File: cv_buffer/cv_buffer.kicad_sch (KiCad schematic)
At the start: 8 parts, among them J1 CV connector, J2 Pot connector, U1 HT7550-1, U2 TLV6001UIDBVR

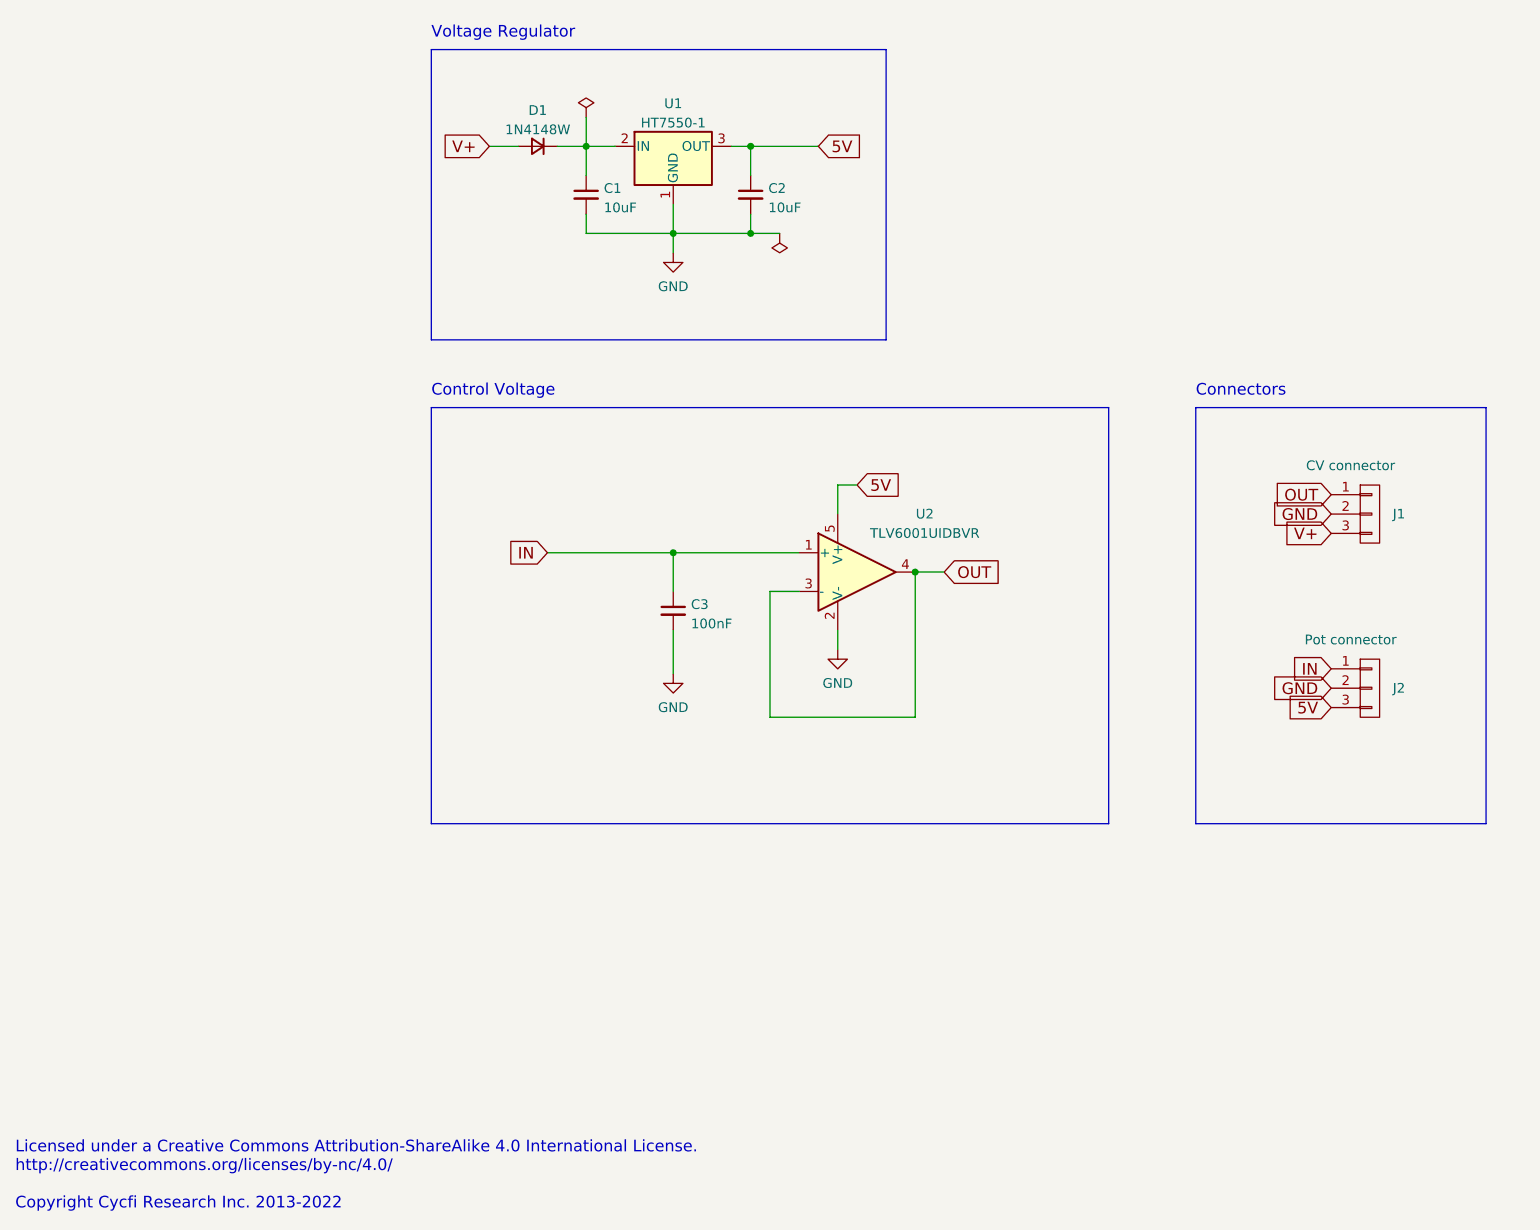
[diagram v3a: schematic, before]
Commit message: CV buffer updates to v3.1 PCB re-layout + various schematic refinements
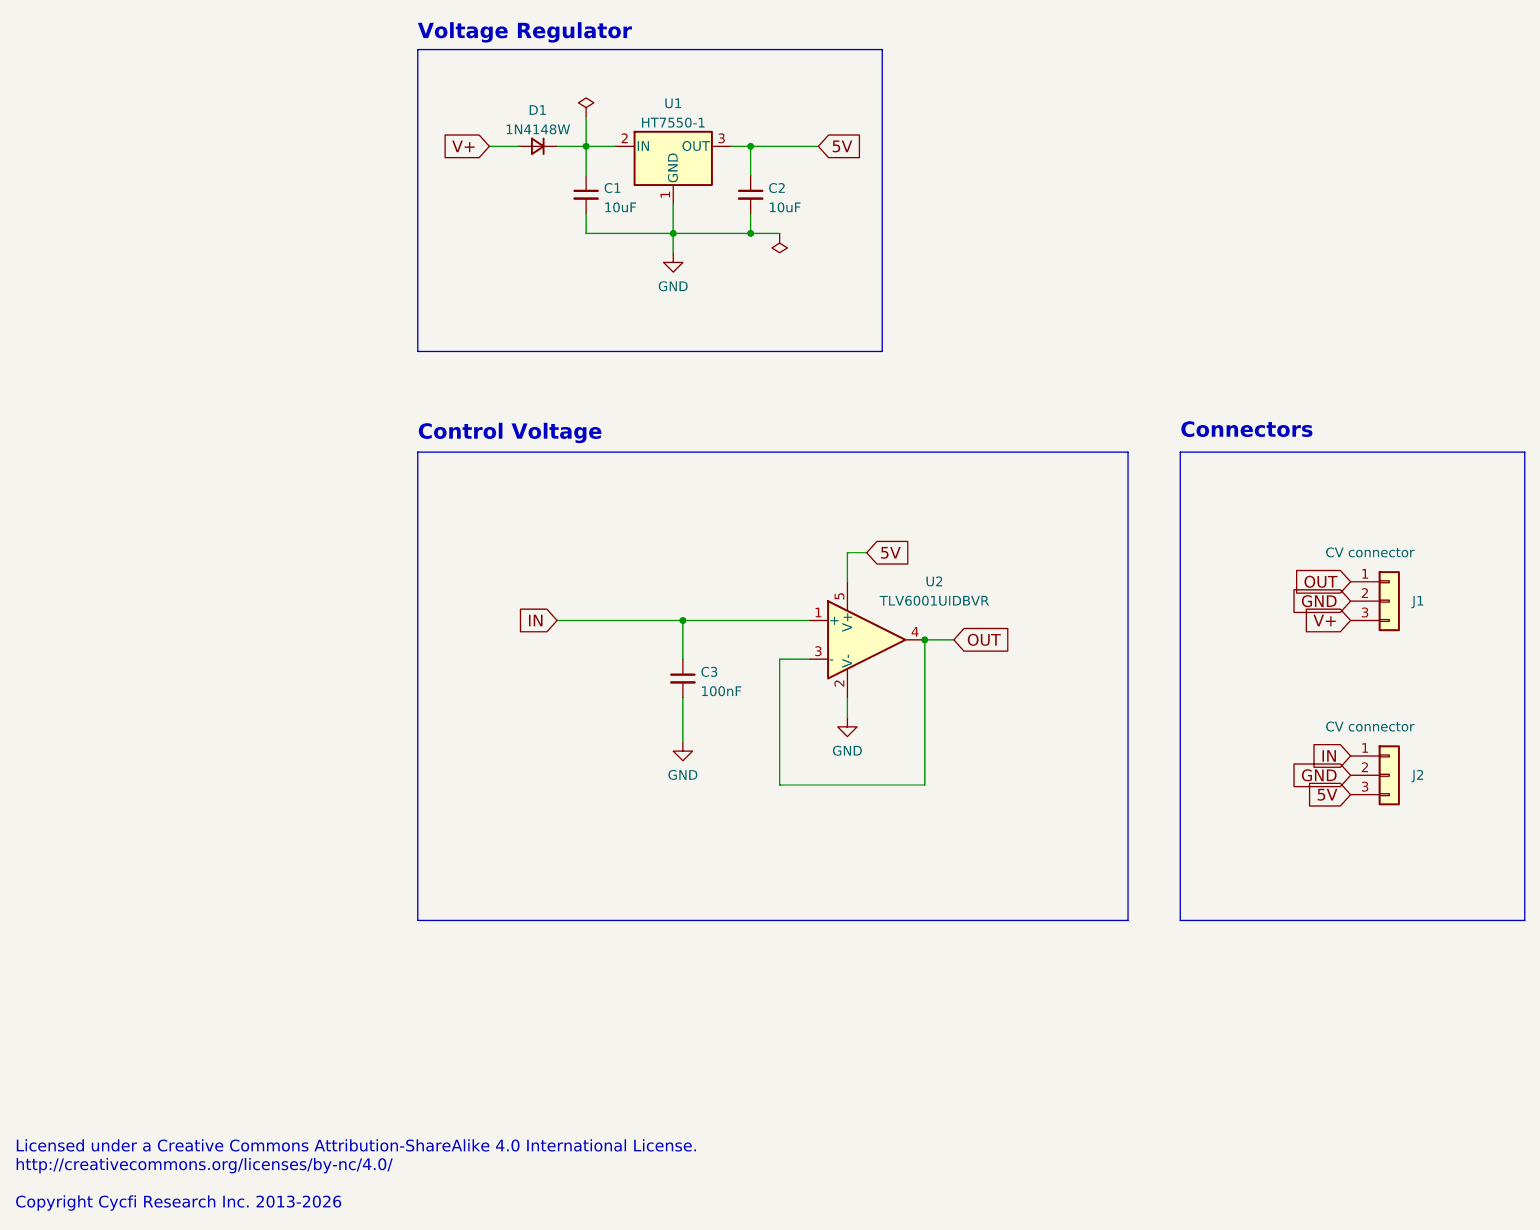
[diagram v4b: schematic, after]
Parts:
- J1: symbol cycfi_library:conn_1x3 -> Connector_Generic:Conn_01x03
- J2: value Pot connector -> CV connector; symbol cycfi_library:conn_1x3 -> Connector_Generic:Conn_01x03
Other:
- note added: "Licensed under a Creative Commons Attribution-ShareAlike 4.0 International License. http://creativecommons.org/licenses/by-nc/4.0/ Copyright Cycfi Research Inc. 2013-2026"
- note removed: "Licensed under a Creative Commons Attribution-ShareAlike 4.0 International License. http://creativecommons.org/licenses/by-nc/4.0/ Copyright Cycfi Research Inc. 2013-2022"
- moved on the sheet: C3, U2

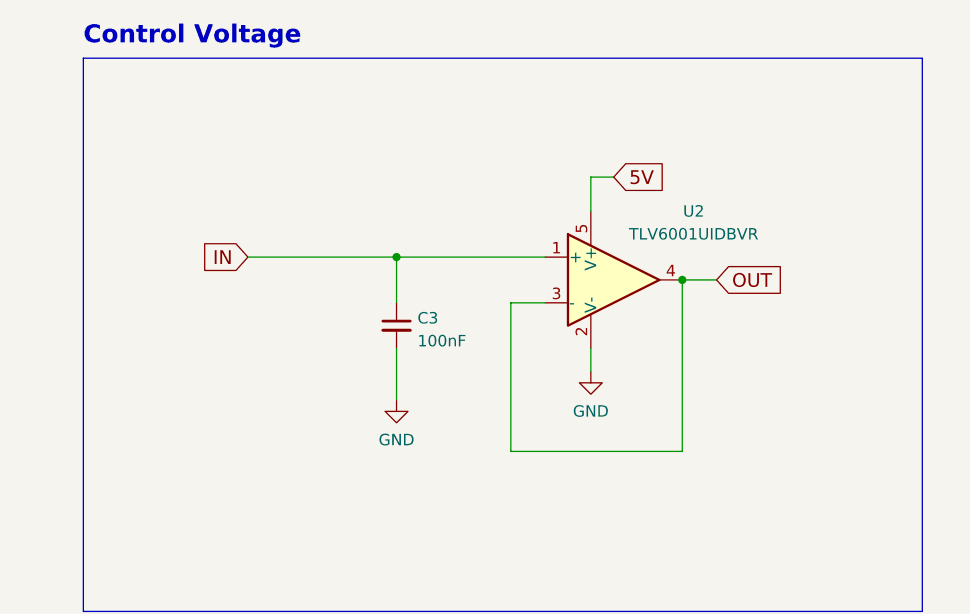
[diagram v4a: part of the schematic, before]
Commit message: Added output 1k resistor
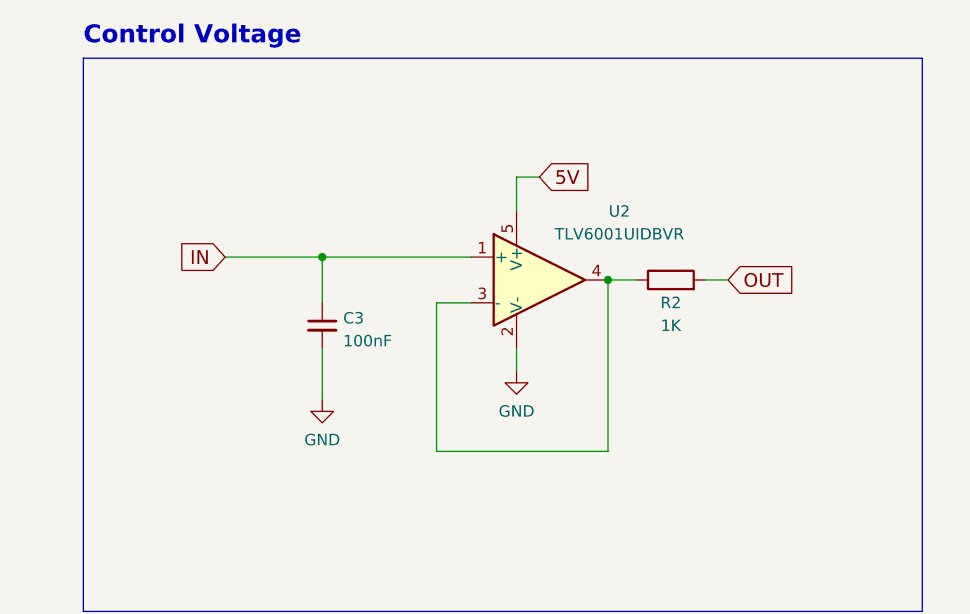
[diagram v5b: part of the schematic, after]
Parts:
- added R2: 1K, Resistor_SMD:R_0402_1005Metric, symbol Device:R
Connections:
- net OUT: now also R2.2; no longer U2.3 (-), U2.4
- new net: R2.1, U2.3 (-), U2.4
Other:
- moved on the sheet: C3, U2
